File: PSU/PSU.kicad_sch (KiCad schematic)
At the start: 2 parts

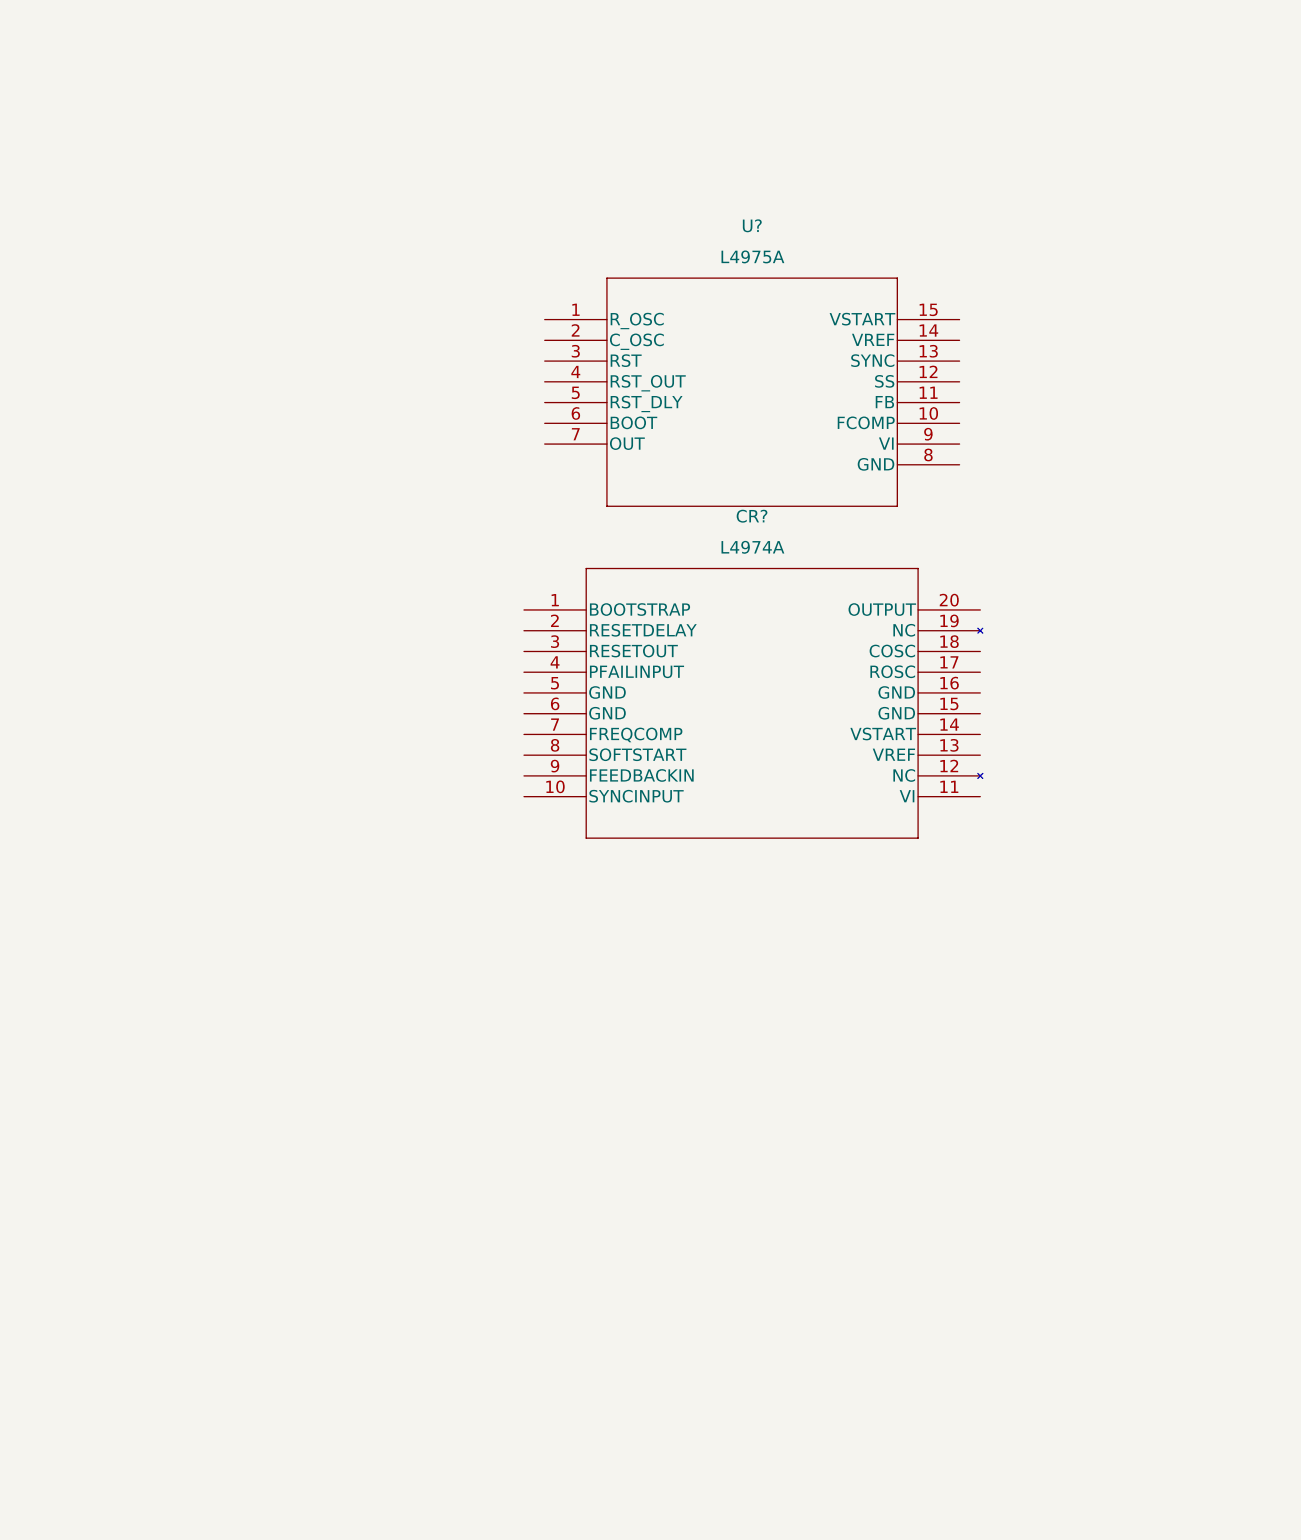
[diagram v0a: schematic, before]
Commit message: Unverified schematic
Drawn the schematic, still need to double check connections. Footprints are yet to be set
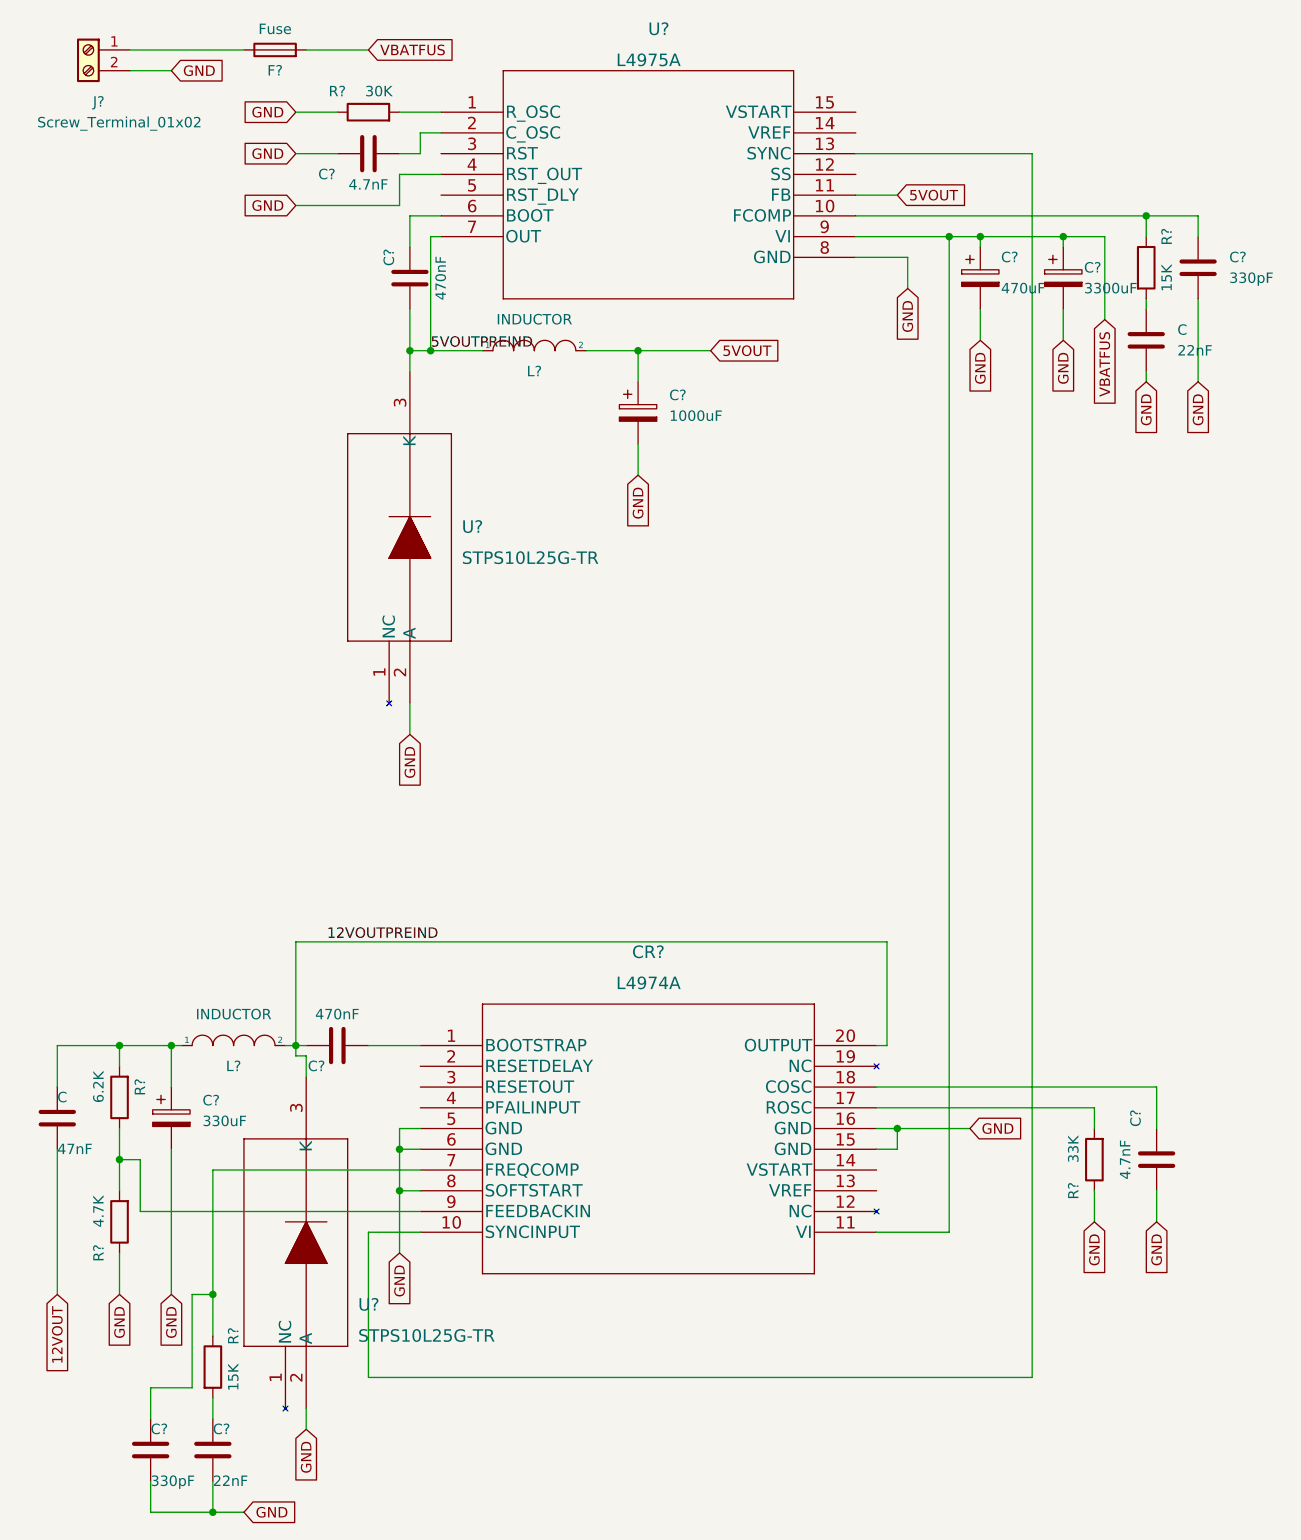
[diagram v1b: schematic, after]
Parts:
- added C: 47nF, symbol Device:C
- added C, C?: 22nF, symbol Device:C
- added C?: 3300uF, symbol Device:C_Polarized
- added C? (x2): 470nF, symbol Device:C
- added C? (x2): 330pF, symbol Device:C
- added C?: 470uF, symbol Device:C_Polarized
- added C? (x2): 4.7nF, symbol Device:C
- added C?: 1000uF, symbol Device:C_Polarized
- added C?: 330uF, symbol Device:C_Polarized
- added F?: Fuse, symbol Device:Fuse
- added J?: Screw_Terminal_01x02, symbol Connector:Screw_Terminal_01x02
- added L? (x2): INDUCTOR, symbol pspice:INDUCTOR
- added R?: 33K, symbol Device:R
- added R?: 6.2K, symbol Device:R
- added R? (x2): 15K, symbol Device:R
- added R?: 30K, symbol Device:R
- added R?: 4.7K, symbol Device:R
- added U? (x2): STPS10L25G-TR, D2PAK_STM, symbol 2022-02-13_20-55-28:STPS10L25G-TR
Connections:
- net at U?.1 (R_OSC): now also R?.2
- net at U?.10 (FCOMP): now also C?.1, R?.1
- net 5VOUT: now reaches U?.11 (FB)
- net 5VOUT: now also C?.1, L?.2
- net at U?.13 (SYNC): now also CR?.10 (SYNCINPUT)
- net at U?.2 (C_OSC): now also C?.2
- net GND: now reaches U?.4 (RST_OUT)
- net GND: now also CR?.15 (GND), CR?.16 (GND), CR?.5 (GND), CR?.6 (GND), CR?.8 (SOFTSTART), U?.8 (GND), C.2, C?.1, C?.2, C?.2, C?.2, C?.2, C?.2, C?.2, C?.2, C?.2, J?.2 (Pin_2), R?.1, R?.1, R?.1, U?.2 (A), U?.2 (A)
- net at U?.6 (BOOT): now also C?.2
- net 5VOUTPREIND: now reaches U?.7 (OUT)
- net 5VOUTPREIND: now also C?.1, L?.1, U?.3 (K)
- net VBATFUS: now reaches U?.9 (VI)
- net VBATFUS: now also CR?.11 (VI), C?.1, C?.1, F?.2
- net at CR?.1 (BOOTSTRAP): now also C?.1
- net at CR?.17 (ROSC): now also R?.2
- net at CR?.18 (COSC): now also C?.1
- net 12VOUTPREIND: now reaches CR?.20 (OUTPUT)
- net 12VOUTPREIND: now also C?.2, L?.2, U?.3 (K)
- net at CR?.7 (FREQCOMP): now also C?.1, R?.1
- net at CR?.9 (FEEDBACKIN): now also R?.1, R?.2
- new net: C?.1, R?.2
- new net: C.1, C?.1, L?.1, R?.2
- new net: C.1, R?.2
- new net: F?.1, J?.1 (Pin_1)
- new net 12VOUT: C.2
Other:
- moved on the sheet: CR?, U?
